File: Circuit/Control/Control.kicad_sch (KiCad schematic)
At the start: 31 parts

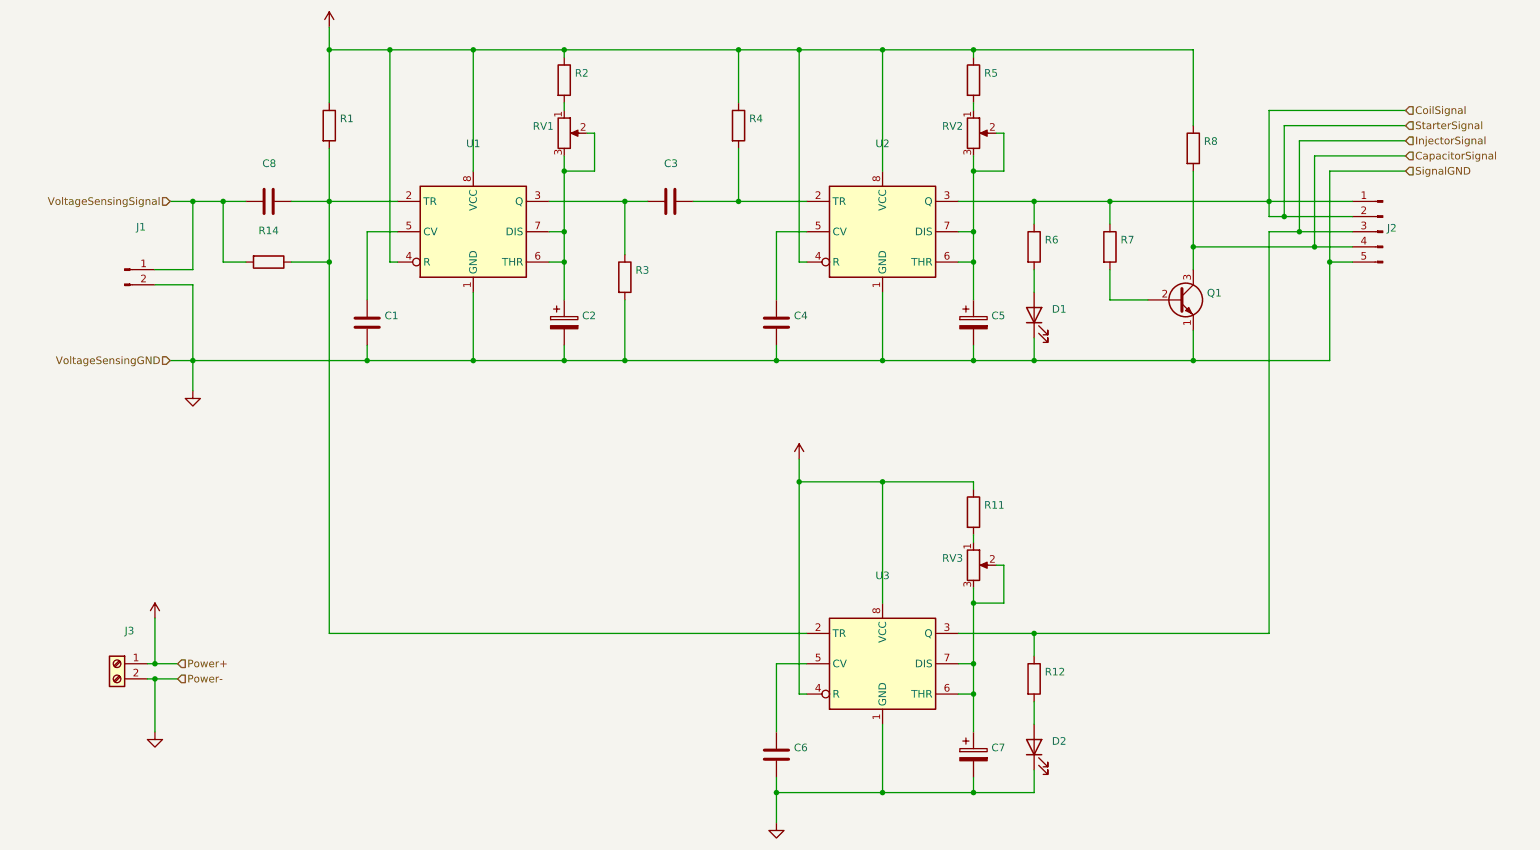
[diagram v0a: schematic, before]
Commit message: [Circuit] A design to use ATtiny85 as a controller
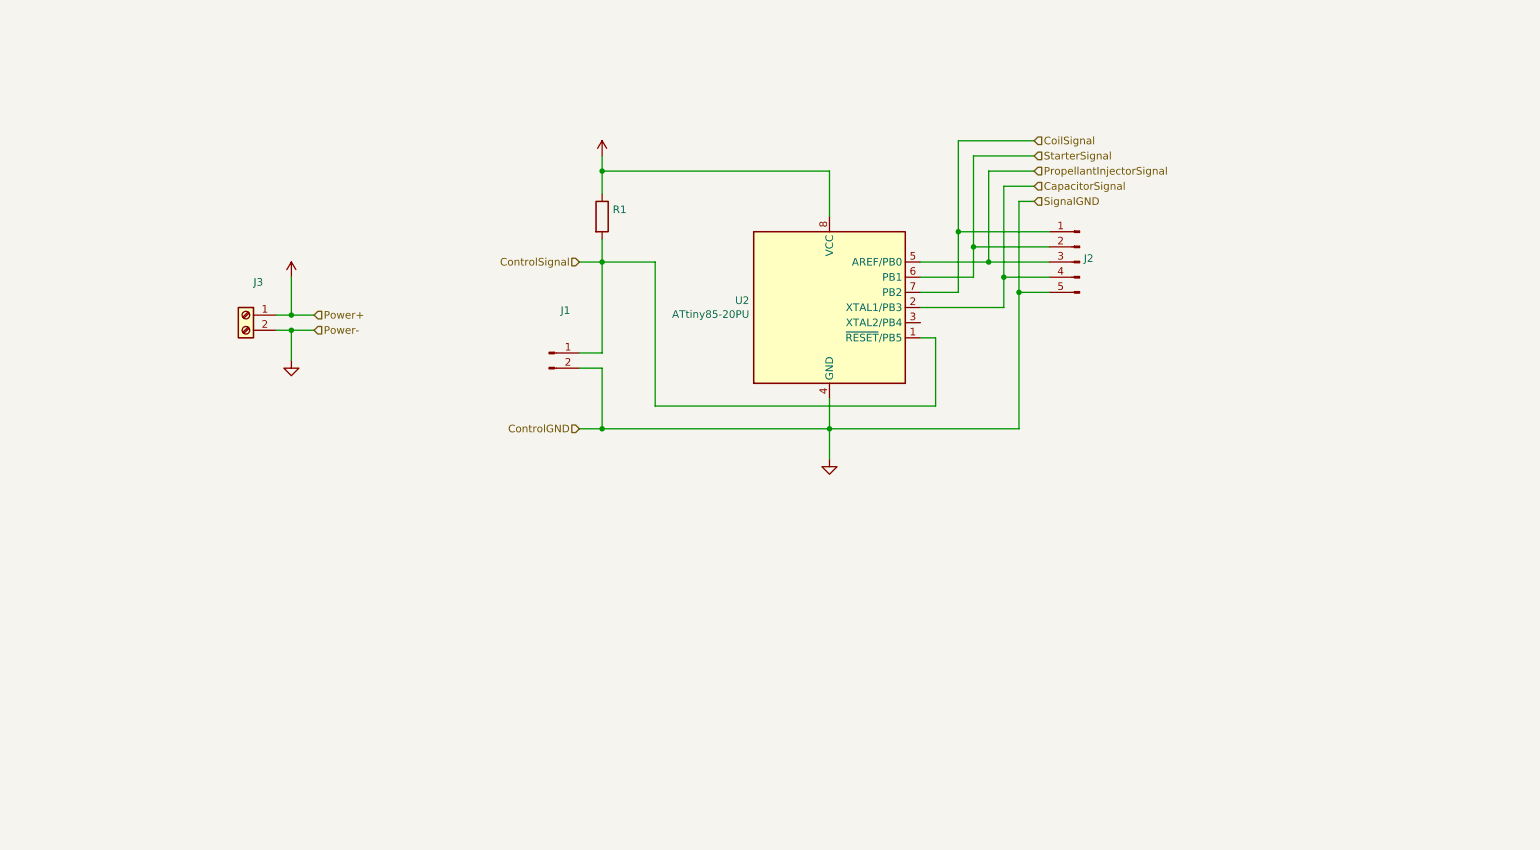
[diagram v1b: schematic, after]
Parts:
- removed C1, C3, C4, C6, C8: (no value), symbol Device:C
- removed C2, C5, C7: (no value), symbol Control-rescue:CP-Device
- removed D1, D2: (no value), symbol Device:LED
- removed Q1: (no value), symbol Transistor_BJT:2N3904
- removed R11, R12, R14, R2, R3, R4, R5, R6, R7, R8: (no value), symbol Device:R
- removed RV1, RV2, RV3: (no value), symbol Control-rescue:R_POT-Device
- removed U1, U2, U3: (no value), symbol Timer:NE555P
- added U2: ATtiny85-20PU, Package_DIP:DIP-8_W7.62mm, symbol MCU_Microchip_ATtiny:ATtiny85-20P
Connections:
- net VoltageSensingSignal is gone; now on net ControlSignal: J1.1 (Pin_1)
- net +5V: now also U2.8 (VCC)
- net CapacitorSignal: now also U2.2 (XTAL1/PB3)
- net CoilSignal: now also U2.7 (PB2); no longer J2.2 (Pin_2)
- net GND: now also U2.4 (GND)
- net ControlSignal: now reaches R1.2
- net ControlSignal: now also U2.1 (~{RESET}/PB5)
- net InjectorSignal renamed PropellantInjectorSignal
- net PropellantInjectorSignal: now also U2.5 (AREF/PB0)
- new net StarterSignal: J2.2 (Pin_2), U2.6 (PB1)
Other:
- moved on the sheet: J1
